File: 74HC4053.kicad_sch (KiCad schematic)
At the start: 3 parts, among them U3 74HC4053, U4 74HC4053

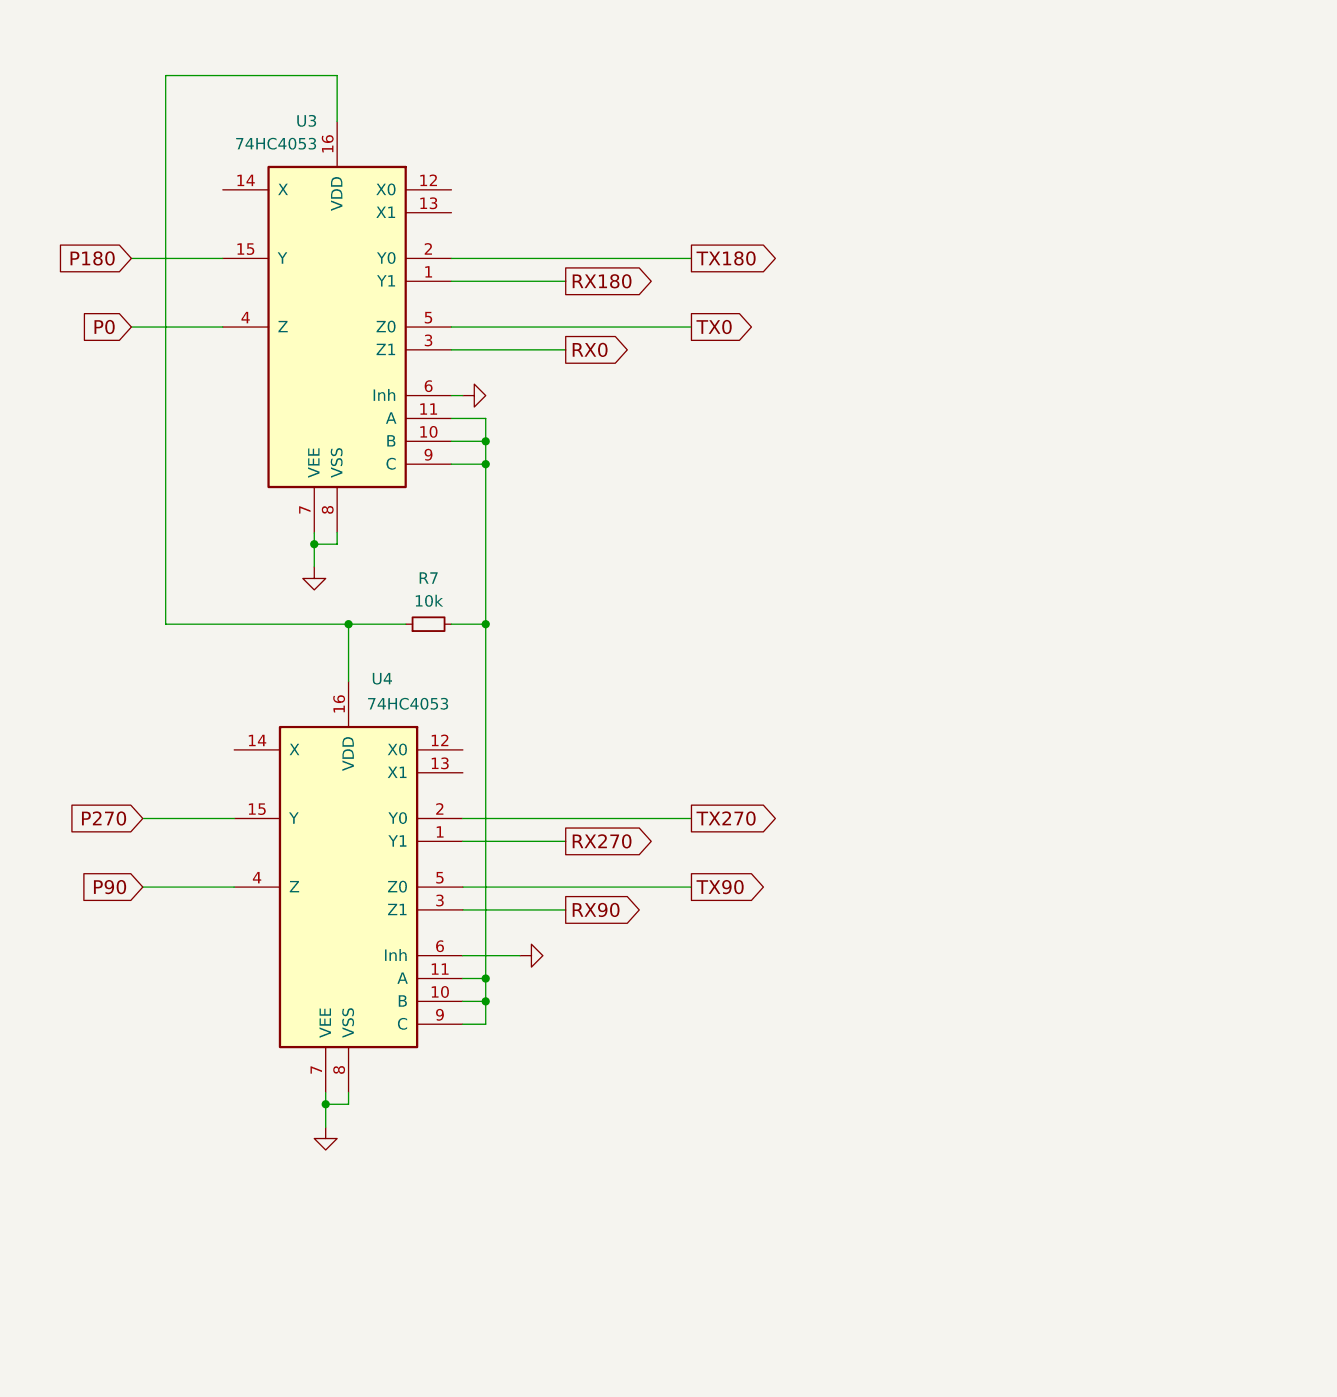
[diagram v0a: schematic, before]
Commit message: schematics mixer, 74HC4053. IF RX needs JLCPCB numbers. PCB update
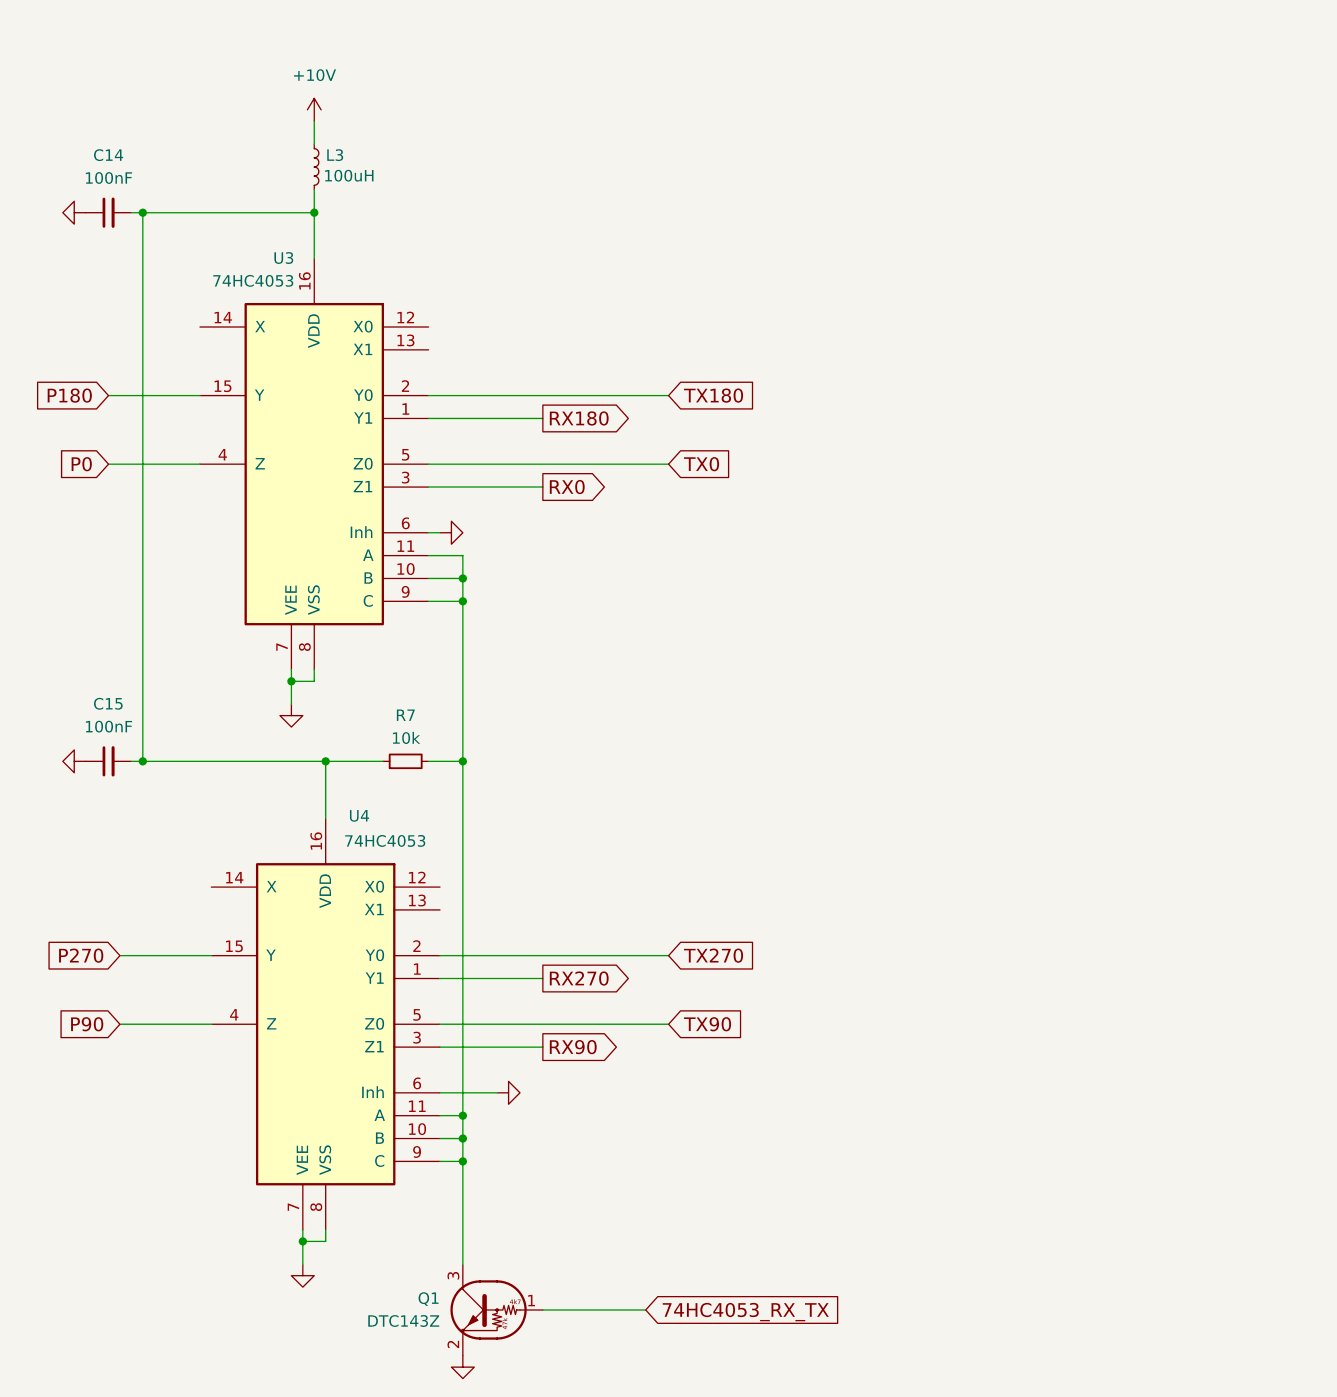
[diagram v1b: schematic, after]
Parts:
- added C14, C15: 100nF, Capacitor_SMD:C_0603_1608Metric_Pad1.08x0.95mm_HandSolder, symbol Device:C_Small
- added L3: 100uH, Inductor_SMD:L_1210_3225Metric_Pad1.42x2.65mm_HandSolder, symbol Device:L_Small
- added Q1: DTC143Z, Package_TO_SOT_SMD:SOT-523, symbol Transistor_BJT:DTC143Z
- U3, U4: footprint (none) -> Package_SO:SO-16_3.9x9.9mm_P1.27mm; JLCPCB (none) -> C9386
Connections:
- net GND: now also C14.1, C15.1, Q1.2 (E)
- net at R7.1, U3.16 (VDD), U4.16 (VDD): now also C14.2, C15.2, L3.2
- net at R7.2, U3.10 (B), U3.11 (A)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: now also Q1.3 (C)
- new net +10V: L3.1
- new net 74HC4053_RX_TX: Q1.1 (B)
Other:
- moved on the sheet: R7, U3, U4

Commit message: some minor changes, IF RX, 74HC4053, page numbers
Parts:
- R7: footprint (none) -> Resistor_SMD:R_0603_1608Metric_Pad0.98x0.95mm_HandSolder; JLCPCB (none) -> C25804
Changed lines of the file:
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@@
 			)
 		)
-		(property "Footprint" ""
+		(property "Footprint" "Resistor_SMD:R_0603_1608Metric_Pad0.98x0.95mm_HandSolder"
 			(at 88.9 106.68 0)
 			(effects
@@
 				)
 				(hide yes)
+			)
+		)
+		(property "JLCPCB" "C25804"
+			(at 88.9 106.68 90)
+			(effects
+				(font
+					(size 1.524 1.524)
+				)
+				(hide yes)

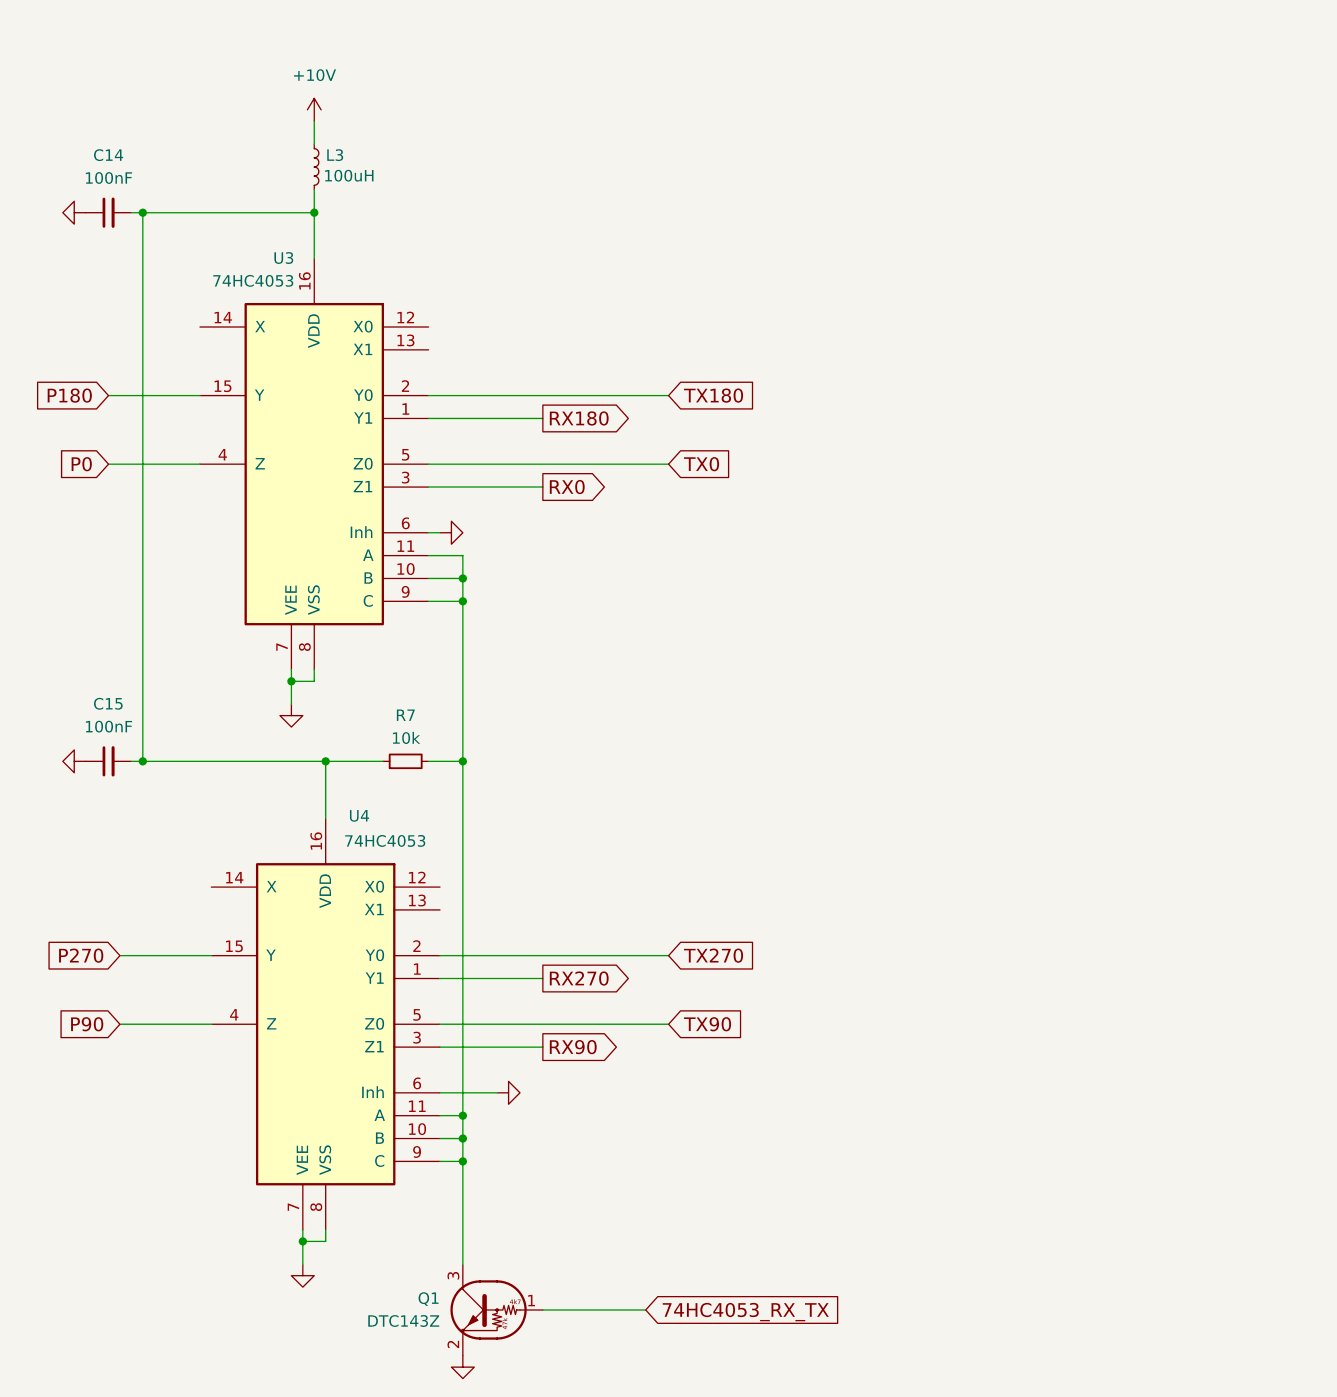
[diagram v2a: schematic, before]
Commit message: finich IF_RX_Schematics, begin MCU, delete *.sch files
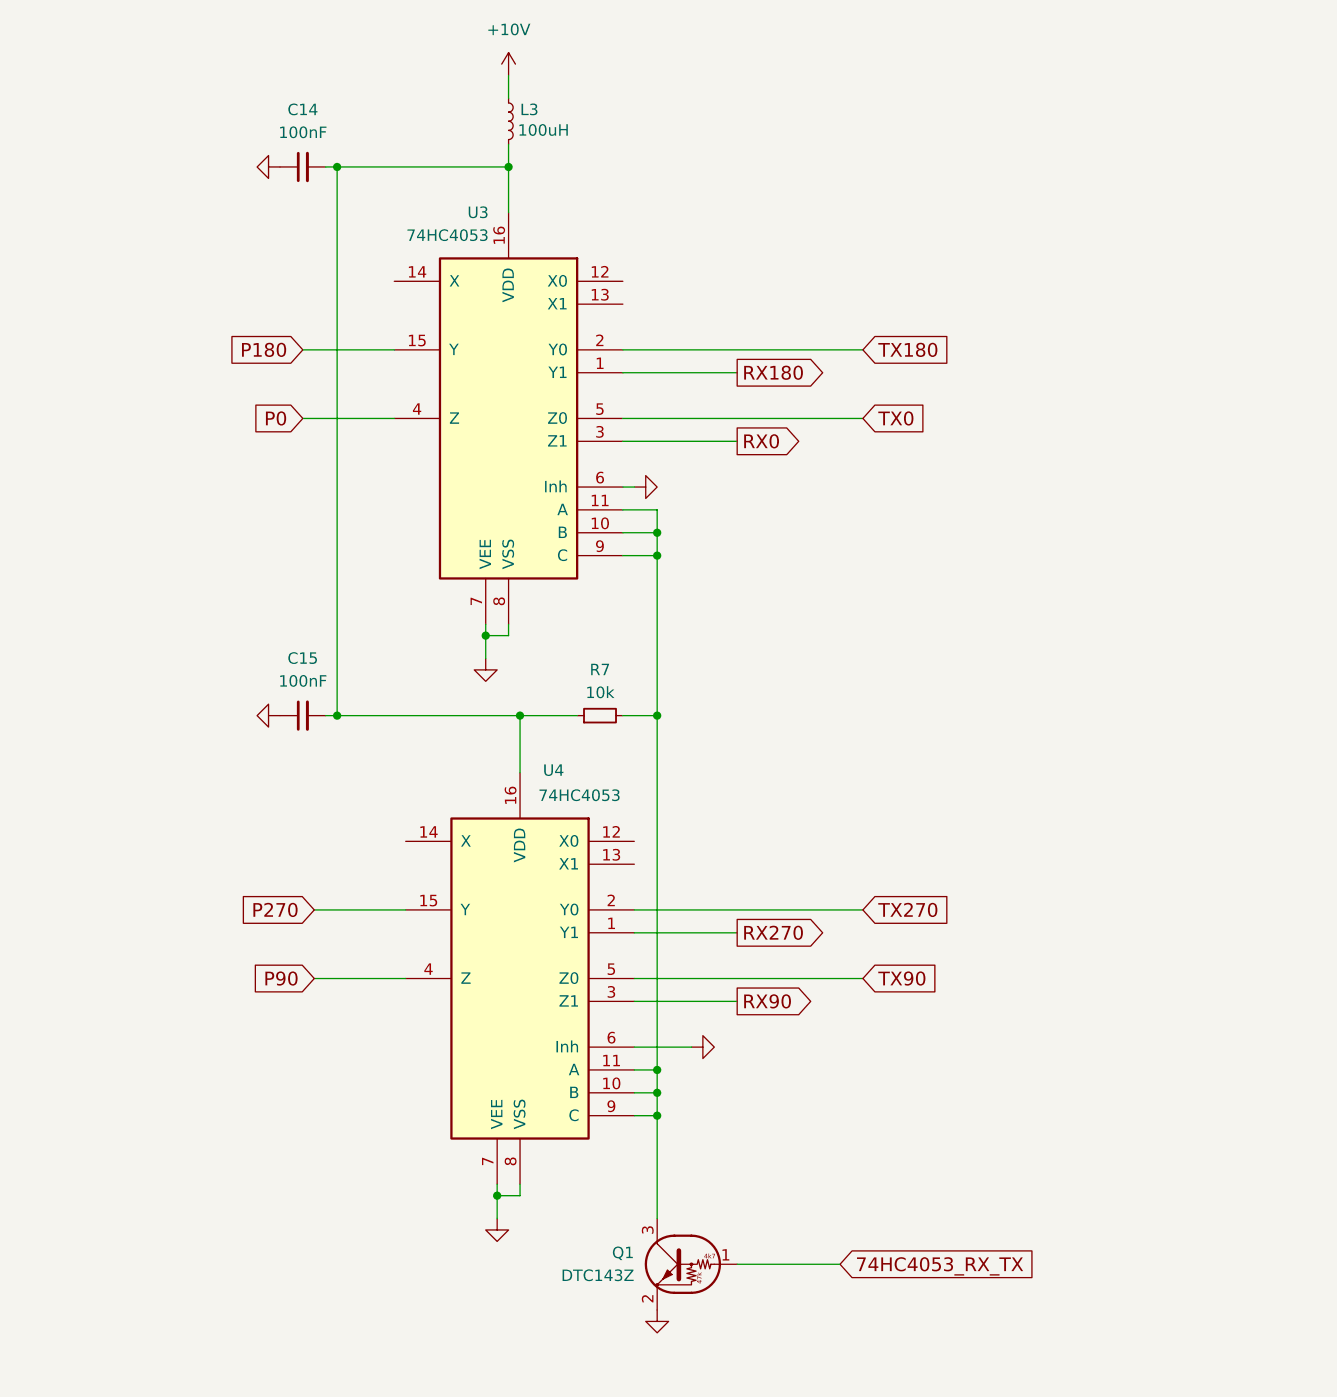
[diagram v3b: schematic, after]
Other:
- moved on the sheet: C14, C15, L3, Q1, R7, U3, U4

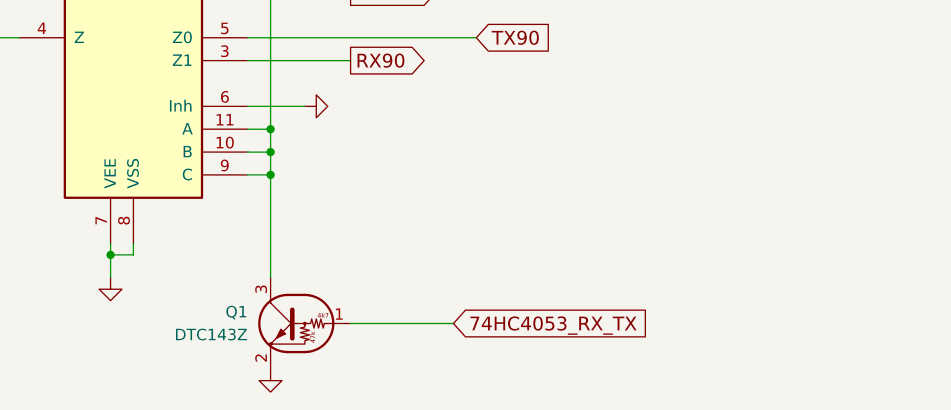
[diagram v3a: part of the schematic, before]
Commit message: add custom footprints, progress on schema and PCB
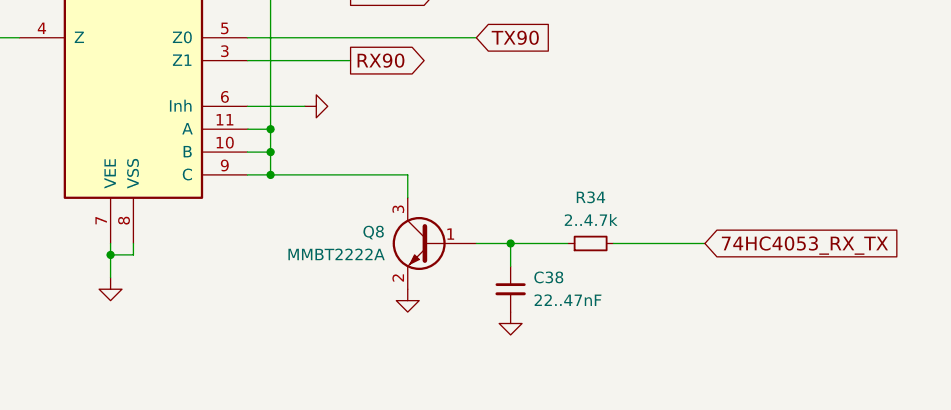
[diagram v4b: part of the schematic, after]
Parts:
- removed Q1: DTC143Z, Package_TO_SOT_SMD:SOT-523, symbol Transistor_BJT:DTC143Z
- added C38: 22..47nF, symbol Device:C_Small
- added Q8: MMBT2222A, Package_TO_SOT_SMD:SOT-23, symbol Transistor_BJT:MMBT2222A
- added R34: 2..4.7k, symbol Device:R_Small
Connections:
- net 74HC4053_RX_TX: now also R34.2
- net GND: now also C38.2, Q8.2 (E)
- net at R7.2, U3.10 (B), U3.11 (A)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: now also Q8.3 (C)
- new net: C38.1, Q8.1 (B), R34.1
